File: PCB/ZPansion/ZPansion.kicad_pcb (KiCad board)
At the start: 2 copper layers, 59.8 x 83.8 mm, 19 parts, among them M1 D24V5F12, M2 TMCSILENTSTEPSTICK, M3 TMCSILENTSTEPSTICK, M4 TMCSILENTSTEPSTICK, T2 0395121002, T3 0395121004, T4 0395121004, T5 0395121004

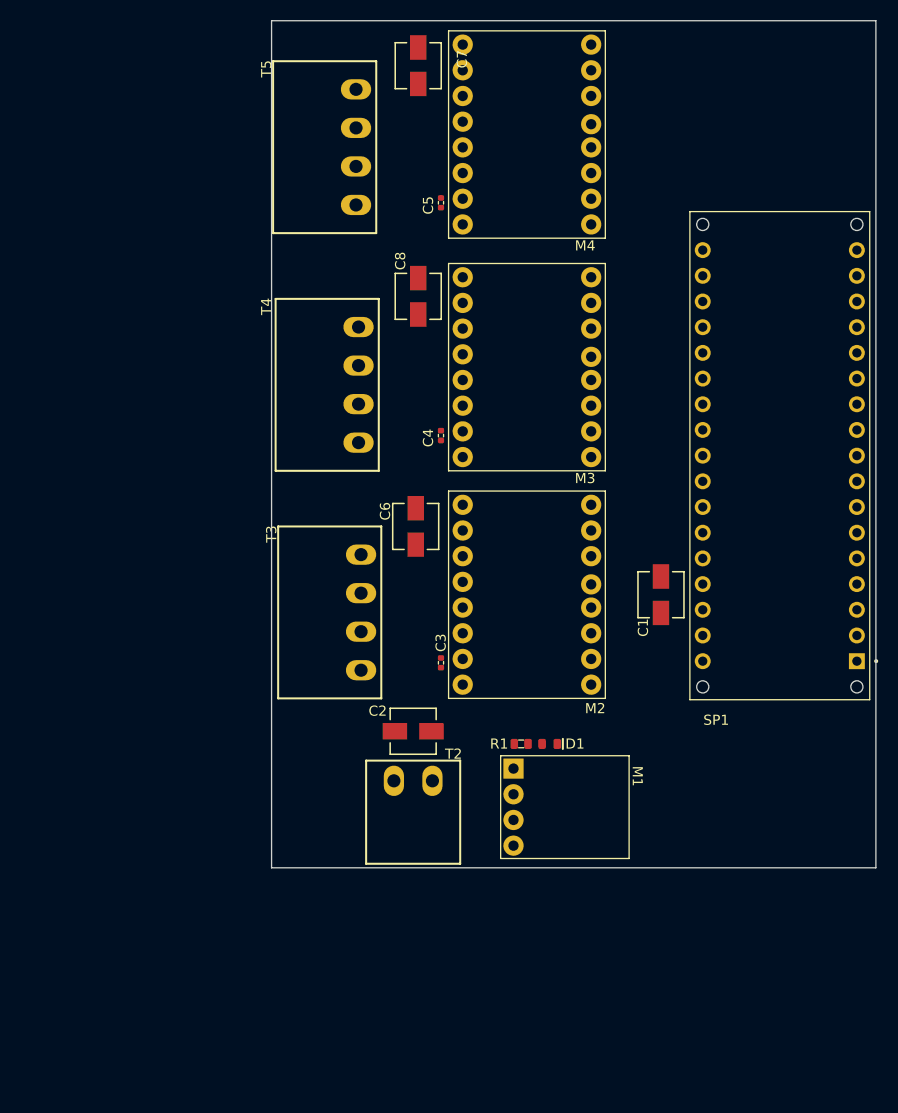
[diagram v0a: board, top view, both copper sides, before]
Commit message: PCB Done
 Finished PCB design and route. Schematic tweaked along the way, termination resistors added to SPI just in case.
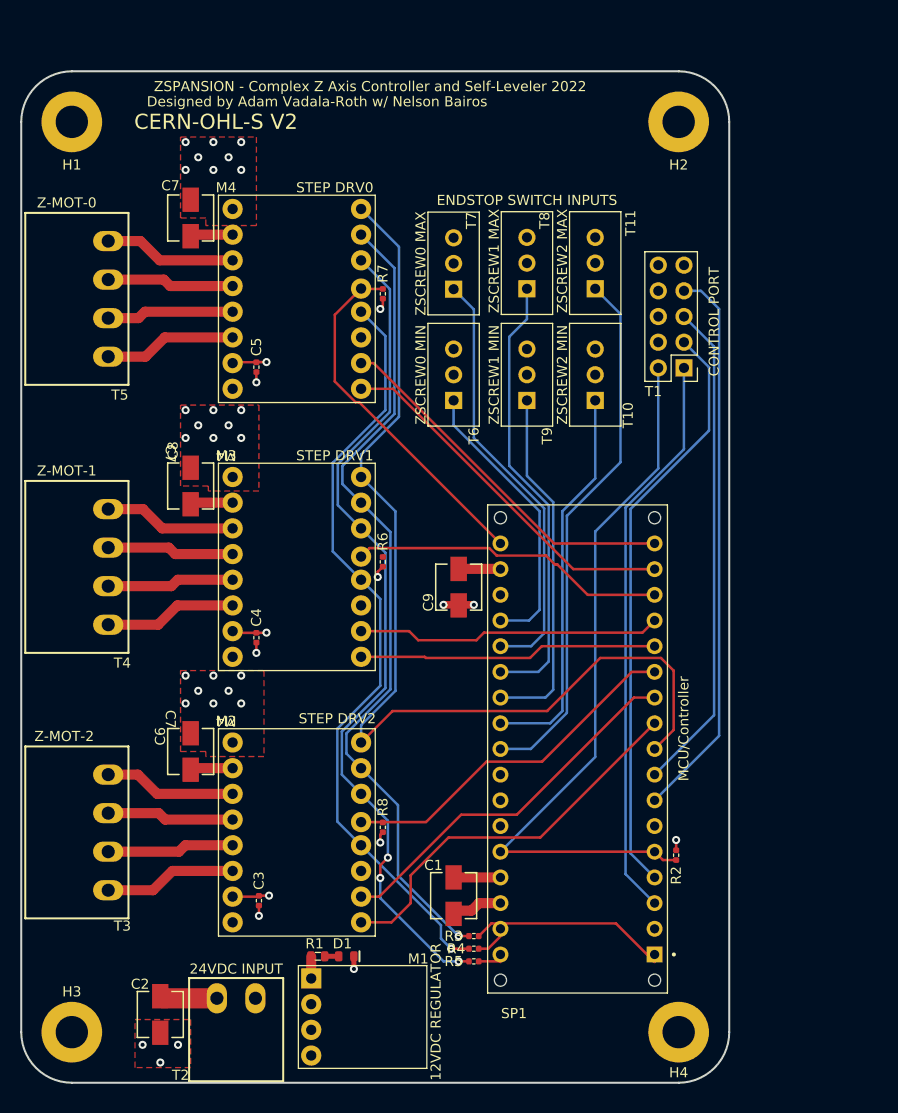
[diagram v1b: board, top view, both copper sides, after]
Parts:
- added C9: UCM1C470MCL1GS, AVR-KiCAD-Lib-Capacitors:UCM1C470MCL1GS, F.Cu at (143.2, 101.0)
- added H1: M3_Plated_Hole, AVR-KiCAD-Lib-Holes_Fasteners:M3_HOLE, F.Cu at (105.0, 55.0)
- added H2: M3_Plated_Hole, AVR-KiCAD-Lib-Holes_Fasteners:M3_HOLE, F.Cu at (165.0, 55.0)
- added H3: M3_Plated_Hole, AVR-KiCAD-Lib-Holes_Fasteners:M3_HOLE, F.Cu at (105.0, 145.0)
- added H4: M3_Plated_Hole, AVR-KiCAD-Lib-Holes_Fasteners:M3_HOLE, F.Cu at (165.0, 145.0)
- added R2: RC0402FR-071KL, AVR-KiCAD-Lib-Resistors:R0402, F.Cu at (164.8, 127.5)
- added R3: RC0402FR-0722RL, AVR-KiCAD-Lib-Resistors:R0402, F.Cu at (144.8, 135.5)
- added R4: RC0402FR-0722RL, AVR-KiCAD-Lib-Resistors:R0402, F.Cu at (144.8, 136.8)
- added R5: RC0402FR-0722RL, AVR-KiCAD-Lib-Resistors:R0402, F.Cu at (144.8, 138.0)
- added R6: RC0402FR-0710KL, AVR-KiCAD-Lib-Resistors:R0402, F.Cu at (135.8, 98.5)
- added R7: RC0402FR-0710KL, AVR-KiCAD-Lib-Resistors:R0402, F.Cu at (135.8, 72.0)
- added R8: RC0402FR-0710KL, AVR-KiCAD-Lib-Resistors:R0402, F.Cu at (135.8, 124.8)
- added T1: PRPC005DAAN-RC, Connector_PinHeader_2.54mm:PinHeader_2x05_P2.54mm_Vertical, F.Cu at (165.5, 79.3)
- added T10: 0705430002, AVR-KiCAD-Lib-Connectors:Shrouded_Pin_Header_Straight_1x03_Pitch2.54mm, F.Cu at (156.8, 82.5)
- added T11: 0705430002, AVR-KiCAD-Lib-Connectors:Shrouded_Pin_Header_Straight_1x03_Pitch2.54mm, F.Cu at (156.8, 71.5)
- added T6: 0705430002, AVR-KiCAD-Lib-Connectors:Shrouded_Pin_Header_Straight_1x03_Pitch2.54mm, F.Cu at (142.8, 82.5)
- added T7: 0705430002, AVR-KiCAD-Lib-Connectors:Shrouded_Pin_Header_Straight_1x03_Pitch2.54mm, F.Cu at (142.8, 71.5)
- added T8: 0705430002, AVR-KiCAD-Lib-Connectors:Shrouded_Pin_Header_Straight_1x03_Pitch2.54mm, F.Cu at (150.0, 71.5)
- added T9: 0705430002, AVR-KiCAD-Lib-Connectors:Shrouded_Pin_Header_Straight_1x03_Pitch2.54mm, F.Cu at (150.0, 82.5)
- moved C2 37.5 mm to (113.8, 143.2), turned to -90 degrees
- moved C1 36.1 mm to (142.8, 131.5)
- moved SP1 35.2 mm to (155.0, 117.0)
- moved T3 33.1 mm to (108.6, 125.2)
- moved M2 32.7 mm to (127.2, 125.2)
- moved C6 31.5 mm to (116.8, 117.2)
- moved T4 30.6 mm to (108.6, 99.0)
- moved M3 30.1 mm to (127.2, 99.0)
- moved C3 29.6 mm to (123.5, 132.0)
- moved C8 29.3 mm to (116.8, 91.0)
- moved D1 29.1 mm to (132.1, 137.5)
- moved R1 29.1 mm to (129.3, 137.5)
- moved M1 28.8 mm to (128.7, 139.7)
- moved T5 28.7 mm to (108.6, 72.5)
- moved M4 28.0 mm to (127.2, 72.5)
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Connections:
- M2 pad 4: /SPI_SDO -> Net-(M2-Pad4)
- M2 pad 6: /SPI_SDI -> Net-(M2-Pad6)
- M2 pad 7: /SPI_SCK -> Net-(M2-Pad7)
- M3 pad 4: /SPI_SDO -> Net-(M2-Pad4)
- M3 pad 6: /SPI_SDI -> Net-(M2-Pad6)
- M3 pad 7: /SPI_SCK -> Net-(M2-Pad7)
- M4 pad 4: /SPI_SDO -> Net-(M2-Pad4)
- M4 pad 6: /SPI_SDI -> Net-(M2-Pad6)
- M4 pad 7: /SPI_SCK -> Net-(M2-Pad7)
- SP1 pad 19: unconnected-(SP1-Pad19) -> +3V3
- SP1 pad 21: unconnected-(SP1-Pad21) -> Net-(SP1-Pad21)
- SP1 pad 22: unconnected-(SP1-Pad22) -> Net-(SP1-Pad22)
- SP1 pad 23: unconnected-(SP1-Pad23) -> Net-(SP1-Pad23)
- SP1 pad 24: unconnected-(SP1-Pad24) -> Net-(SP1-Pad24)
- SP1 pad 25: unconnected-(SP1-Pad25) -> Net-(SP1-Pad25)
- SP1 pad 26: unconnected-(SP1-Pad26) -> Net-(SP1-Pad26)
- SP1 pad 9: unconnected-(SP1-Pad9) -> /ENABLE
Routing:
- net GNDREF: track 0.00 -> 312.2 mm
- net /ENABLE: track 0.00 -> 102.1 mm
- net Net-(M2-Pad6): track 0.00 -> 83.7 mm, vias 0 -> 3
- net Net-(M2-Pad7): track 0.00 -> 82.2 mm, vias 0 -> 1
- net Net-(M2-Pad4): track 0.00 -> 76.3 mm, vias 0 -> 1
- net /SYS_RESET: track 0.00 -> 72.0 mm
- net /UART_RX: track 0.00 -> 58.1 mm
- net /UART_TX: track 0.00 -> 56.5 mm
- net /MASTER_STEP: track 0.00 -> 55.4 mm
- net Net-(SP1-Pad26): track 0.00 -> 53.2 mm
- net /MASTER_DIR: track 0.00 -> 49.0 mm
- net Net-(SP1-Pad23): track 0.00 -> 44.4 mm
- net Net-(SP1-Pad22): track 0.00 -> 42.6 mm
- net /DRV1_DIR: track 0.00 -> 38.8 mm
- net Net-(SP1-Pad25): track 0.00 -> 38.7 mm
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- added copper zone on In1.Cu, net +12V
- added copper zone on F.Cu, net +24V
- added copper zone on In1.Cu, net +24V
- added copper zone on In1.Cu, net +3V3
- added copper zone on F.Cu, net GND
- added copper zone on In2.Cu, net GND
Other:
- board size 59.8 x 83.8 mm -> 70 x 100 mm
- copper layers 2 -> 4
- board text added: "12VDC REGULATOR"
- board text added: "24VDC INPUT"
- board text added: "C7"
- board text added: "CERN-OHL-S V2"
- board text added: "CONTROL PORT"
- board text added: "Designed by Adam Vadala-Roth w/ Nelson Bairos"
- board text added: "ENDSTOP SWITCH INPUTS"
- board text added: "M4"
- board text added: "MCU/Controller"
- board text added: "STEP DRV0"
- board text added: "STEP DRV1"
- board text added: "STEP DRV2"
- board text added: "Z-MOT-0"
- board text added: "Z-MOT-1"
- board text added: "Z-MOT-2"
- board text added: "ZSCREW0 MAX"
- board text added: "ZSCREW0 MIN"
- board text added: "ZSCREW1 MAX"
- board text added: "ZSCREW1 MIN"
- board text added: "ZSCREW2 MAX"
- board text added: "ZSCREW2 MIN"
- board text added: "ZSPANSION - Complex Z Axis Controller and Self-Leveler 2022"
